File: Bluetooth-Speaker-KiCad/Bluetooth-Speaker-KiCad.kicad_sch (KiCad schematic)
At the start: 33 parts, among them J1 Screw_Terminal_01x02, J2 USB_C_Receptacle_USB2.0_14P, J3 Screw_Terminal_01x02, Q1 Q_PMOS_DSG, SW1 SW_Push, SW2 SW_Push, U1 RT6150B-33GQW, U2 MAX98357A, U4 TPD4E02B04DQA, U5 ESP32-C3-WROOM-02, U6 MAX1811

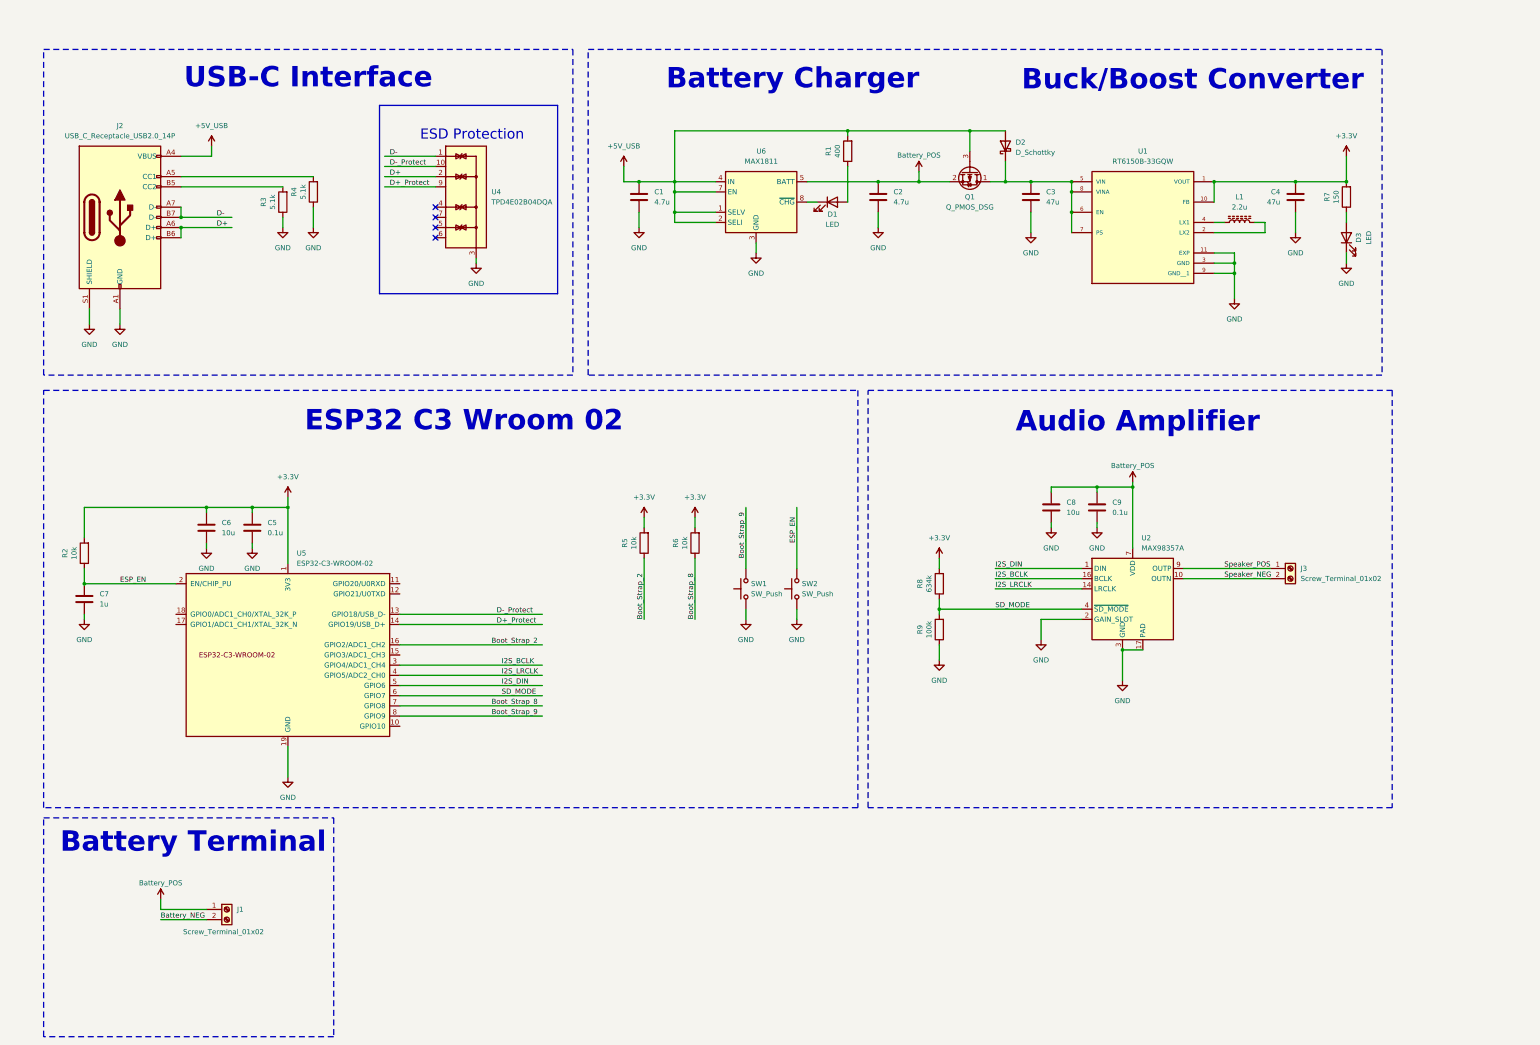
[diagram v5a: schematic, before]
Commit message: Updated layout
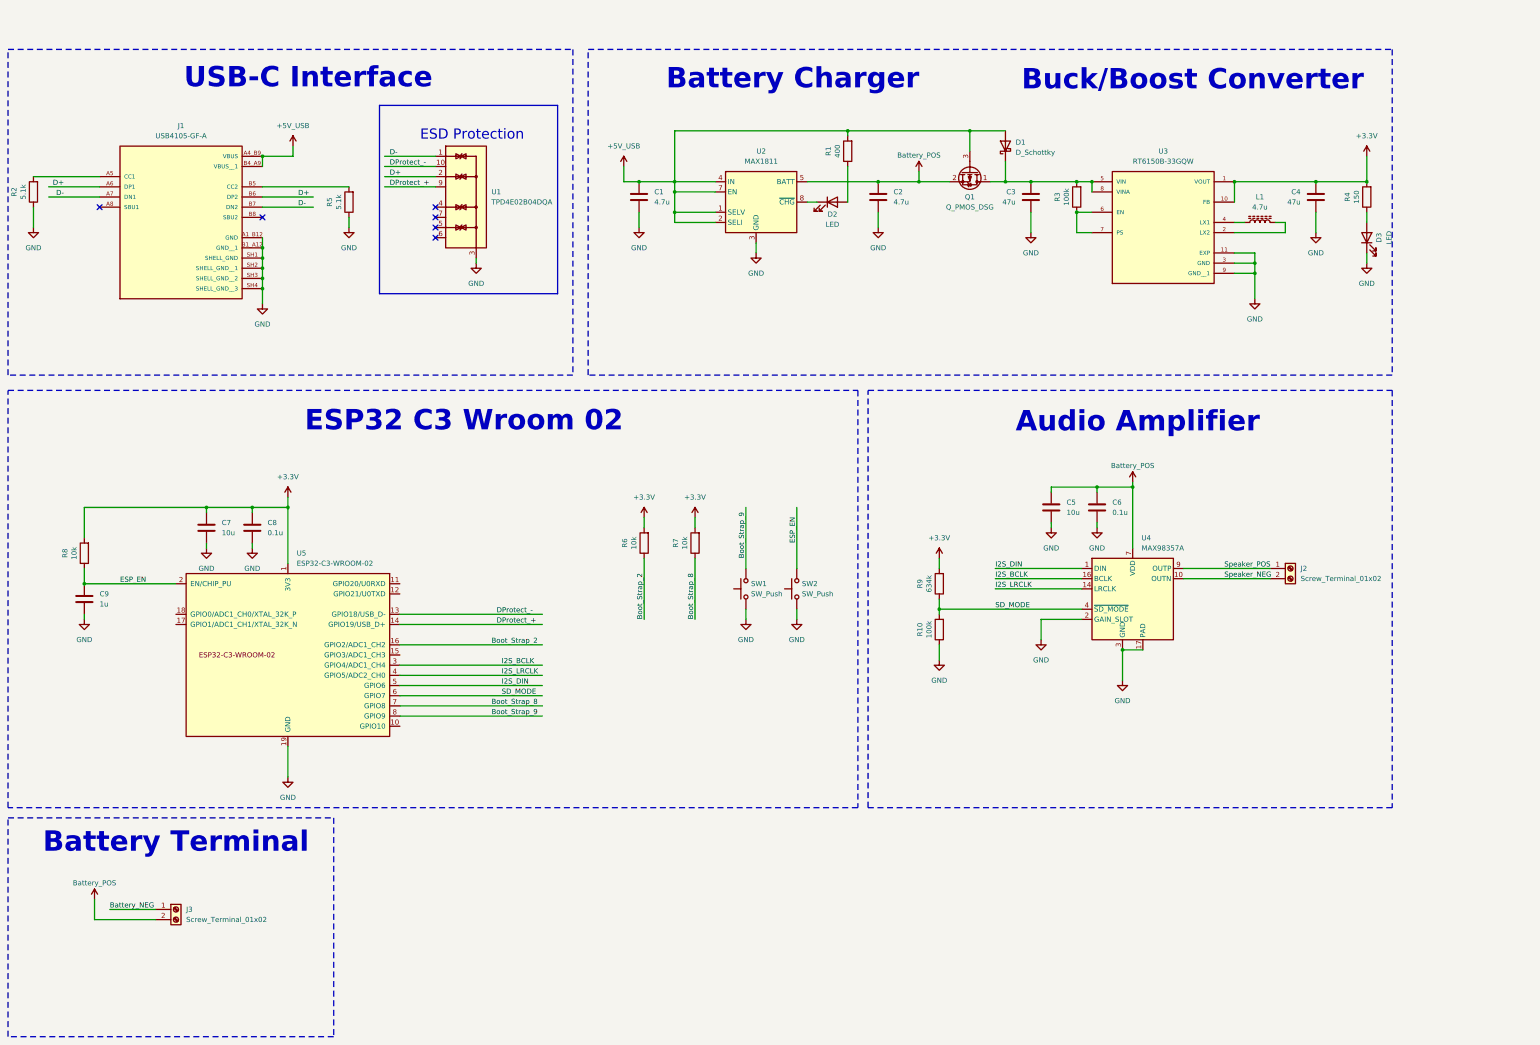
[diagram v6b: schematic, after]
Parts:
- removed J1: Screw_Terminal_01x02, symbol Connector:Screw_Terminal_01x02
- removed J2: USB_C_Receptacle_USB2.0_14P, symbol Connector:USB_C_Receptacle_USB2.0_14P
- added J1: USB4105-GF-A, USB4105_GF_A:GCT_USB4105-GF-A, symbol USB4105-GF-A:USB4105-GF-A
- added J2: Screw_Terminal_01x02, TerminalBlock_Phoenix:TerminalBlock_Phoenix_MKDS-1,5-2-5.08_1x02_P5.08mm_Horizontal, symbol Connector:Screw_Terminal_01x02
- added R3: 100k, Resistor_SMD:R_0603_1608Metric_Pad0.98x0.95mm_HandSolder, symbol Device:R
- J3: footprint (none) -> TerminalBlock_Phoenix:TerminalBlock_Phoenix_MKDS-1,5-2-5.08_1x02_P5.08mm_Horizontal
- L1: value 2.2u -> 4.7u
- Q1: footprint (none) -> DMG2305UX_7 (1):SOT91P240X110-3N_DMG2305UX-7
- renumbered C8 to C5, C9 to C6, C6 to C7, C5 to C8, C7 to C9, D2 to D1, D1 to D2, R9 to R10, R4 to R2, R7 to R4, R3 to R5, R5 to R6, R6 to R7, R2 to R8, R8 to R9, U4 to U1, U6 to U2, U1 to U3, U2 to U4
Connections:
- net +5V_USB: now also J1.A4_B9 (VBUS), J1.B4_A9 (VBUS__1)
- net Battery_NEG: now also J3.1 (Pin_1)
- net Battery_POS: now also J3.2 (Pin_2)
- net D+: now also J1.A6 (DP1), J1.B6 (DP2)
- net D-: now also J1.A7 (DN1), J1.B7 (DN2)
- net GND: now also J1.A1_B12 (GND), J1.B1_A12 (GND__1), J1.SH1 (SHELL_GND), J1.SH2 (SHELL_GND__1), J1.SH3 (SHELL_GND__2), J1.SH4 (SHELL_GND__3)
- net Speaker_NEG: now also J2.2 (Pin_2); no longer J3.2 (Pin_2)
- net Speaker_POS: now also J2.1 (Pin_1); no longer J3.1 (Pin_1)
- net at R2.2: now also J1.A5 (CC1)
- net at R5.2: now also J1.B5 (CC2)
- net at C3.1, D1.1 (K), Q1.1 (D)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: now also R3.2; no longer U3.6 (EN), U3.7 (PS)
- net D+_Protect renamed DProtect_+
- net D-_Protect renamed DProtect_-
- new net: R3.1, U3.6 (EN), U3.7 (PS)
- no-connect marks 4 -> 6
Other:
- moved on the sheet: C4, D3, L1, R2, R4, R5, U3

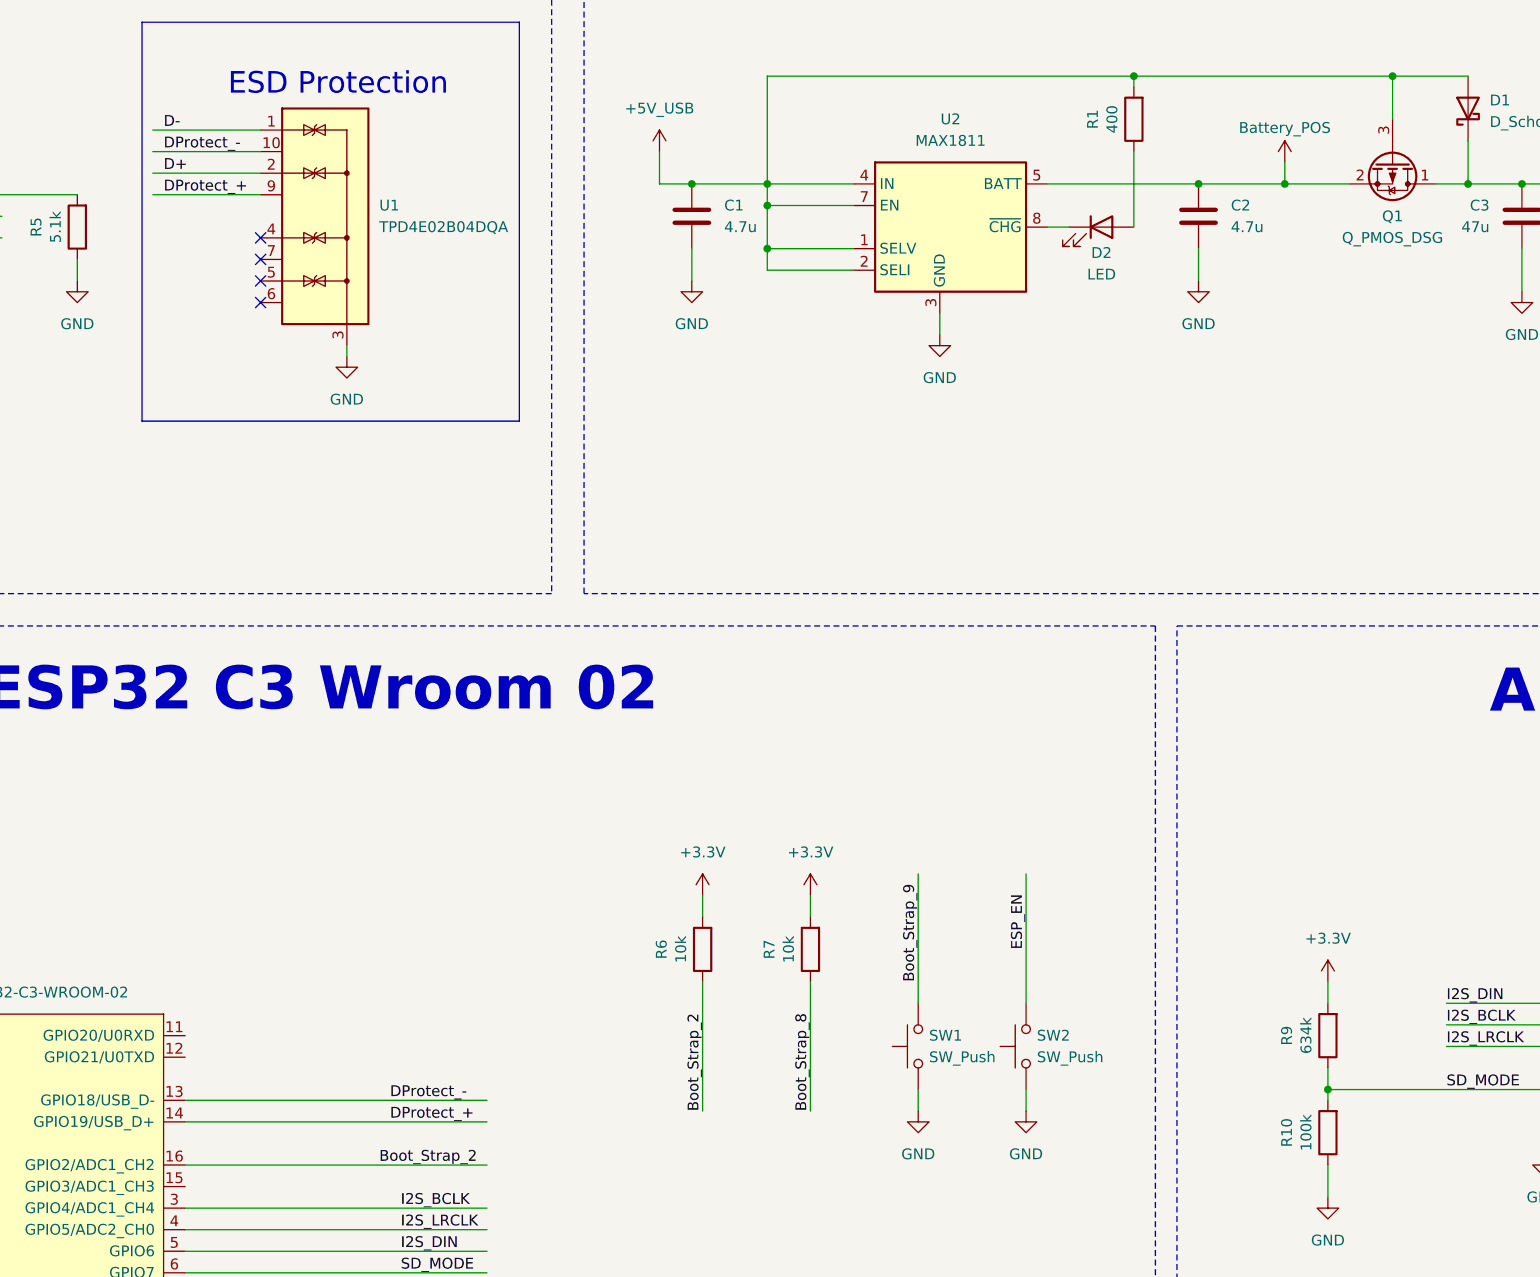
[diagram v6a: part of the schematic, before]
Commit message: Updated layout
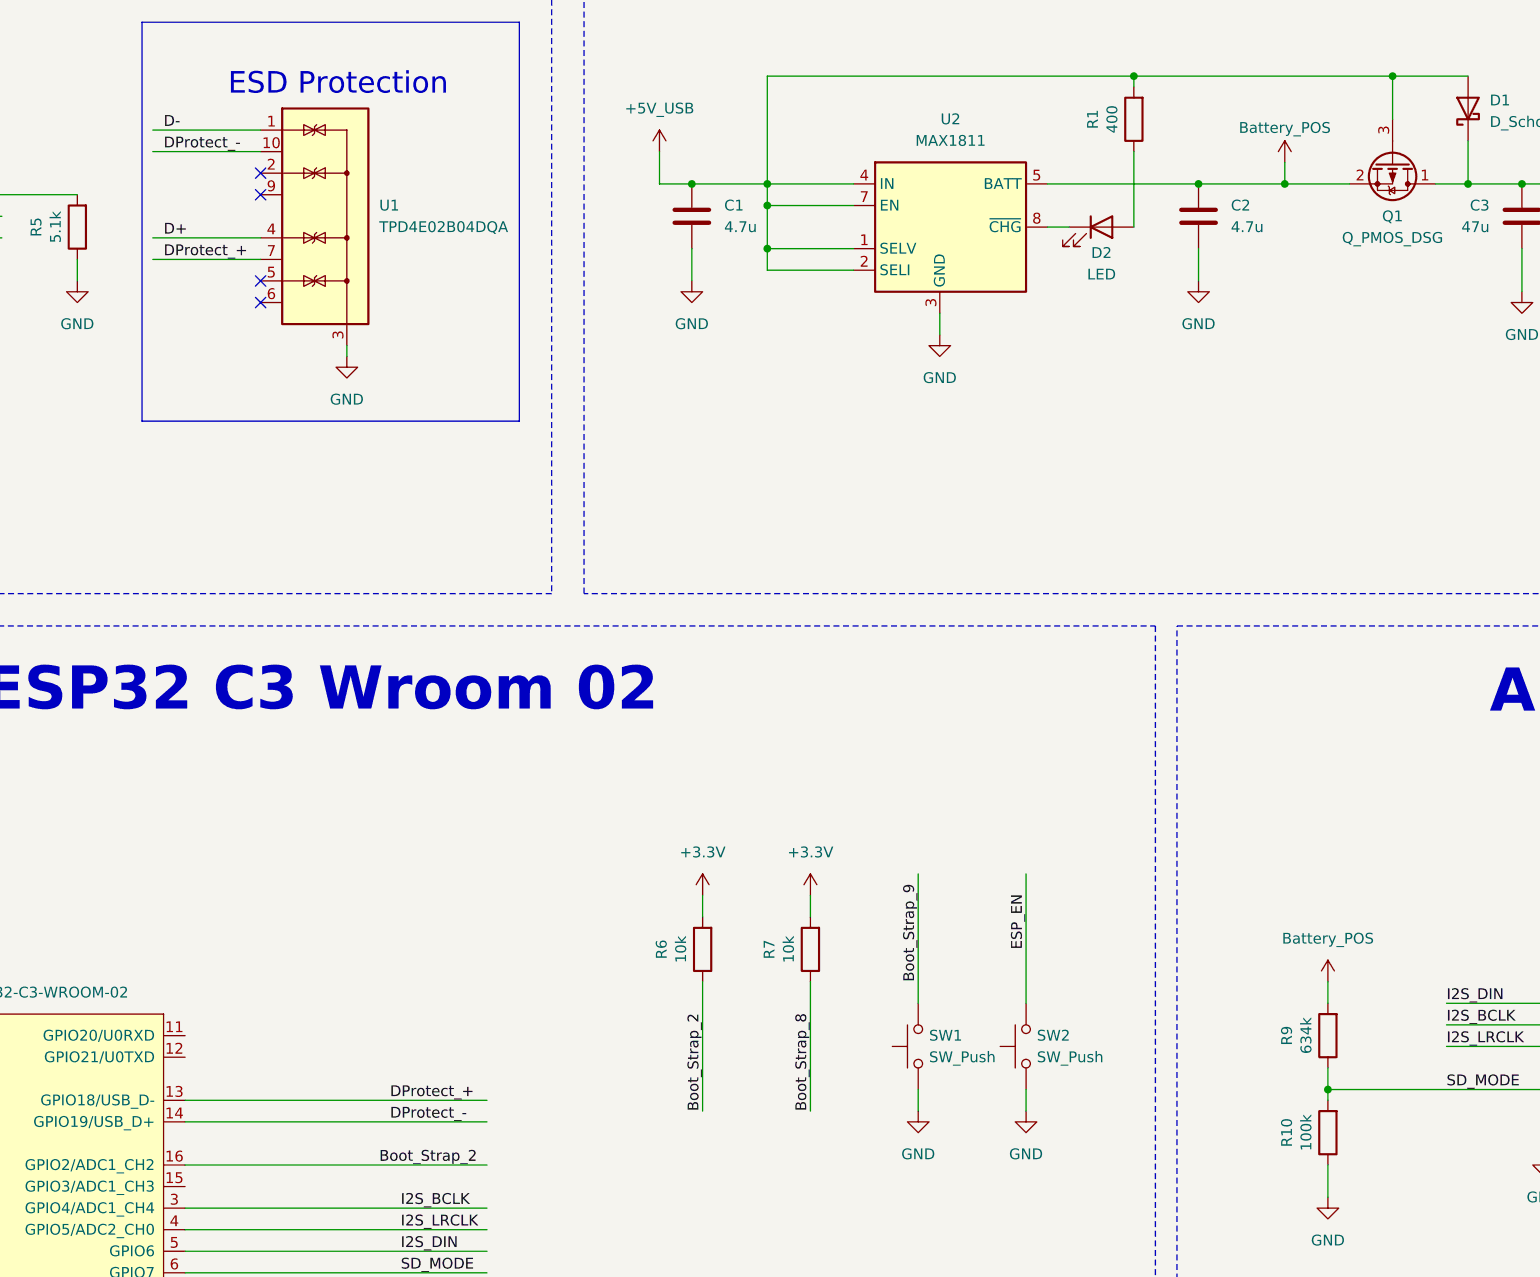
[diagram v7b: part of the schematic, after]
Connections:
- net +3.3V: no longer R9.2
- net Battery_POS: now also R9.2
- net D+: now also U1.4 (IO3); no longer U1.2 (IO2)
- net DProtect_+: now also U1.7 (NC), U5.13 (GPIO18/USB_D-); no longer U1.9 (NC), U5.14 (GPIO19/USB_D+)
- net DProtect_-: now also U5.14 (GPIO19/USB_D+); no longer U5.13 (GPIO18/USB_D-)
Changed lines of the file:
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@@
 	)
 	(no_connect
-		(at 127 67.31)
+		(at 83.82 69.85)
 	)
 	(no_connect
-		(at 83.82 69.85)
+		(at 127 59.69)
 	)
 	(no_connect
@@
 	)
 	(no_connect
-		(at 127 69.85)
+		(at 127 62.23)
 	)
 	(no_connect
@@
 	(wire
 		(pts
-			(xy 114.3 59.69) (xy 127 59.69)
-		)
-		(stroke
-			(width 0)
-			(type default)
-		)
-	)
-	(wire
-		(pts
 			(xy 298.45 177.8) (xy 298.45 185.42)
 		)
@@
 	(wire
 		(pts
+			(xy 114.3 67.31) (xy 127 67.31)
+		)
+		(stroke
+			(width 0)
+			(type default)
+		)
+	)
+	(wire
+		(pts
 			(xy 83.82 62.23) (xy 105.41 62.23)
 		)
@@
 	(wire
 		(pts
-			(xy 114.3 62.23) (xy 127 62.23)
-		)
-		(stroke
-			(width 0)
-			(type default)
-		)
-	)
-	(wire
-		(pts
 			(xy 118.11 189.23) (xy 153.67 189.23)
 		)
@@
 	(wire
 		(pts
+			(xy 114.3 69.85) (xy 127 69.85)
+		)
+		(stroke
+			(width 0)
+			(type default)
+		)
+	)
+	(wire
+		(pts
 			(xy 118.11 184.15) (xy 153.67 184.15)
 		)
@@
 		)
 	)
-	(label "I2S_DIN"
-		(at 143.51 186.69 0)
+	(label "DProtect_+"
+		(at 142.24 168.91 0)
 		(fields_autoplaced yes)
 		(effects
@@
 		)
 	)
-	(label "DProtect_-"
-		(at 115.57 57.15 0)
+	(label "I2S_DIN"
+		(at 143.51 186.69 0)
 		(fields_autoplaced yes)
 		(effects
@@
 		)
 	)
-	(label "Boot_Strap_8"
-		(at 140.97 191.77 0)
+	(label "DProtect_-"
+		(at 115.57 57.15 0)
 		(fields_autoplaced yes)
 		(effects
@@
 		)
 	)
-	(label "DProtect_+"
-		(at 142.24 171.45 0)
+	(label "Boot_Strap_8"
+		(at 140.97 191.77 0)
 		(fields_autoplaced yes)
 		(effects
@@
 		)
 	)
-	(label "DProtect_-"
-		(at 142.24 168.91 0)
-		(fields_autoplaced yes)
-		(effects
-			(font
-				(size 1.27 1.27)
-			)
-			(justify left bottom)
-		)
-	)
 	(label "I2S_BCLK"
 		(at 143.51 181.61 0)
@@
 	)
 	(label "DProtect_+"
-		(at 115.57 62.23 0)
+		(at 115.57 69.85 0)
 		(fields_autoplaced yes)
 		(effects
@@
 		)
 	)
+	(label "DProtect_-"
+		(at 142.24 171.45 0)
+		(fields_autoplaced yes)
+		(effects
+			(font
+				(size 1.27 1.27)
+			)
+			(justify left bottom)
+		)
+	)
 	(label "I2S_BCLK"
 		(at 266.7 160.02 0)
@@
 	)
 	(label "D+"
-		(at 115.57 59.69 0)
+		(at 92.71 64.77 0)
 		(fields_autoplaced yes)
 		(effects
@@
 		)
 	)
-	(label "D+"
-		(at 92.71 64.77 0)
+	(label "I2S_LRCLK"
+		(at 143.51 184.15 0)
 		(fields_autoplaced yes)
 		(effects
@@
 	)
 	(label "I2S_LRCLK"
-		(at 143.51 184.15 0)
+		(at 266.7 162.56 0)
 		(fields_autoplaced yes)
 		(effects
@@
 		)
 	)
-	(label "I2S_LRCLK"
-		(at 266.7 162.56 0)
+	(label "D+"
+		(at 115.57 67.31 0)
 		(fields_autoplaced yes)
 		(effects
@@
 			)
 		)
-		(property "Value" "+3.3V"
+		(property "Value" "Battery_POS"
 			(at 252.73 149.86 0)
 			(effects
